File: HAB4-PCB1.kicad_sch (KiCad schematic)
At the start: 15 parts, among them J1 Barrel_Jack_Switch

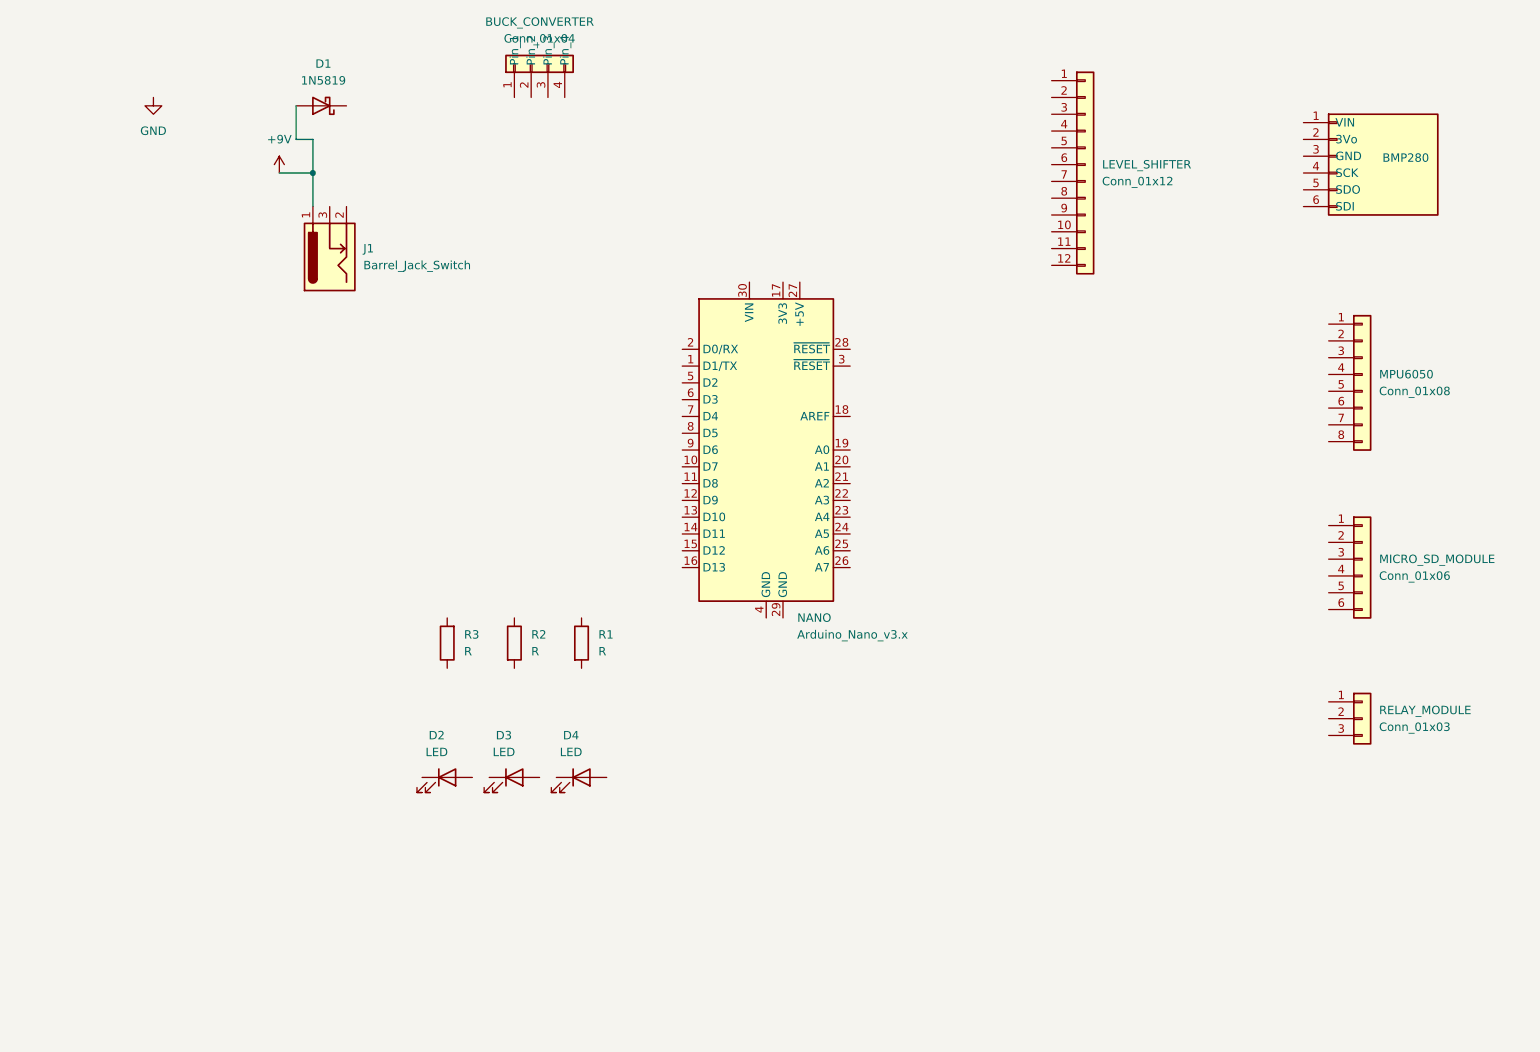
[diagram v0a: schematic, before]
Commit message: Connected modules
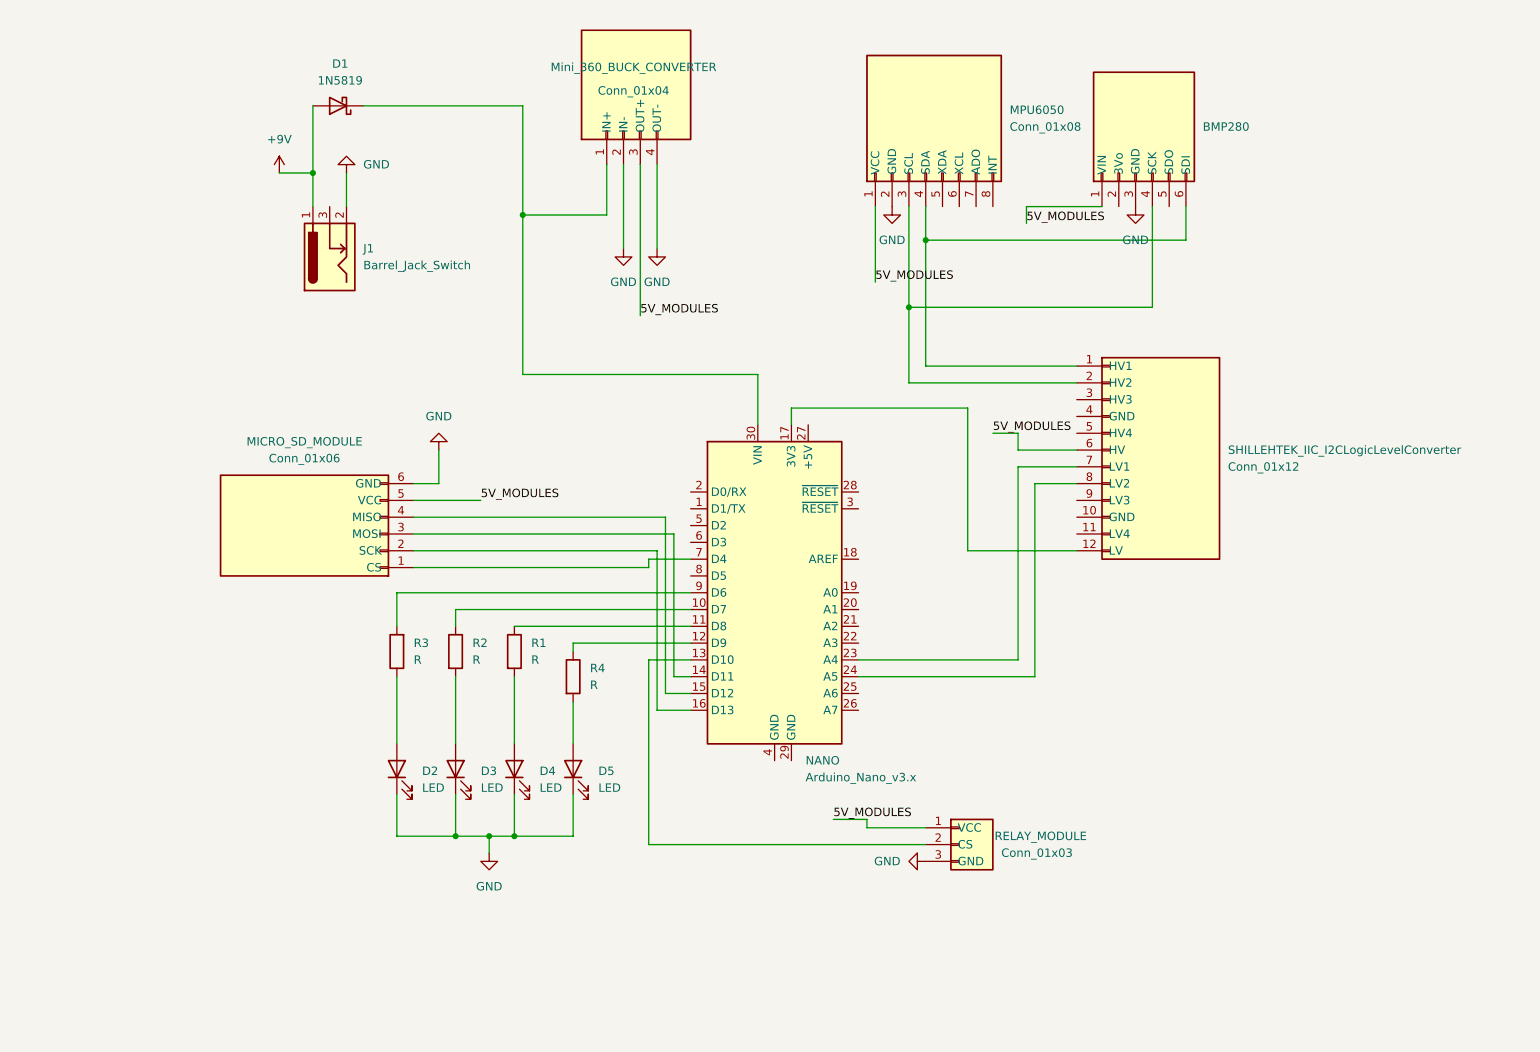
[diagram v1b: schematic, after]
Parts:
- added D5: LED, symbol Device:LED
- added R4: R, symbol Device:R
- renumbered BUCK_CONVERTER to Mini_360_BUCK_CONVERTER, LEVEL_SHIFTER to SHILLEHTEK_IIC_I2CLogicLevelConverter
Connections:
- net GND: now also BMP280.3 (GND), D2.1 (K), D3.1 (K), D4.1 (K), J1.2, MICRO_SD_MODULE.6 (GND), MPU6050.2 (GND), Mini_360_BUCK_CONVERTER.2 (IN-), Mini_360_BUCK_CONVERTER.4 (OUT-), RELAY_MODULE.3 (GND), D5.1 (K)
- net at R1.1: now also NANO.11 (D8)
- net at R1.2: now also D4.2 (A)
- net at SHILLEHTEK_IIC_I2CLogicLevelConverter.1 (HV1): now also BMP280.6 (SDI), MPU6050.4 (SDA)
- net at SHILLEHTEK_IIC_I2CLogicLevelConverter.12 (LV): now also NANO.17 (3V3)
- net at SHILLEHTEK_IIC_I2CLogicLevelConverter.2 (HV2): now also BMP280.4 (SCK), MPU6050.3 (SCL)
- net 5V_MODULES: now reaches SHILLEHTEK_IIC_I2CLogicLevelConverter.6 (HV)
- net 5V_MODULES: now also BMP280.1 (VIN), MICRO_SD_MODULE.5 (VCC), MPU6050.1 (VCC), Mini_360_BUCK_CONVERTER.3 (OUT+), RELAY_MODULE.1 (VCC)
- net at SHILLEHTEK_IIC_I2CLogicLevelConverter.7 (LV1): now also NANO.23 (A4)
- net at SHILLEHTEK_IIC_I2CLogicLevelConverter.8 (LV2): now also NANO.24 (A5)
- net at D1.1 (K): now also Mini_360_BUCK_CONVERTER.1 (IN+), NANO.30 (VIN)
- net at R2.1: now also NANO.10 (D7)
- net at R2.2: now also D3.2 (A)
- net at MICRO_SD_MODULE.1 (CS): now also NANO.7 (D4)
- net at MICRO_SD_MODULE.2 (SCK): now also NANO.16 (D13)
- net at MICRO_SD_MODULE.3 (MOSI): now also NANO.14 (D11)
- net at MICRO_SD_MODULE.4 (MISO): now also NANO.15 (D12)
- net at R3.1: now also D2.2 (A)
- net at R3.2: now also NANO.9 (D6)
- net at RELAY_MODULE.2 (CS): now also NANO.13 (D10)
- net at NANO.12 (D9): now also R4.1
- new net: D5.2 (A), R4.2
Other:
- moved on the sheet: BMP280, D1, D2, D3, D4, Mini_360_BUCK_CONVERTER, NANO, R1, R2, R3

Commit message: footprints and connections update
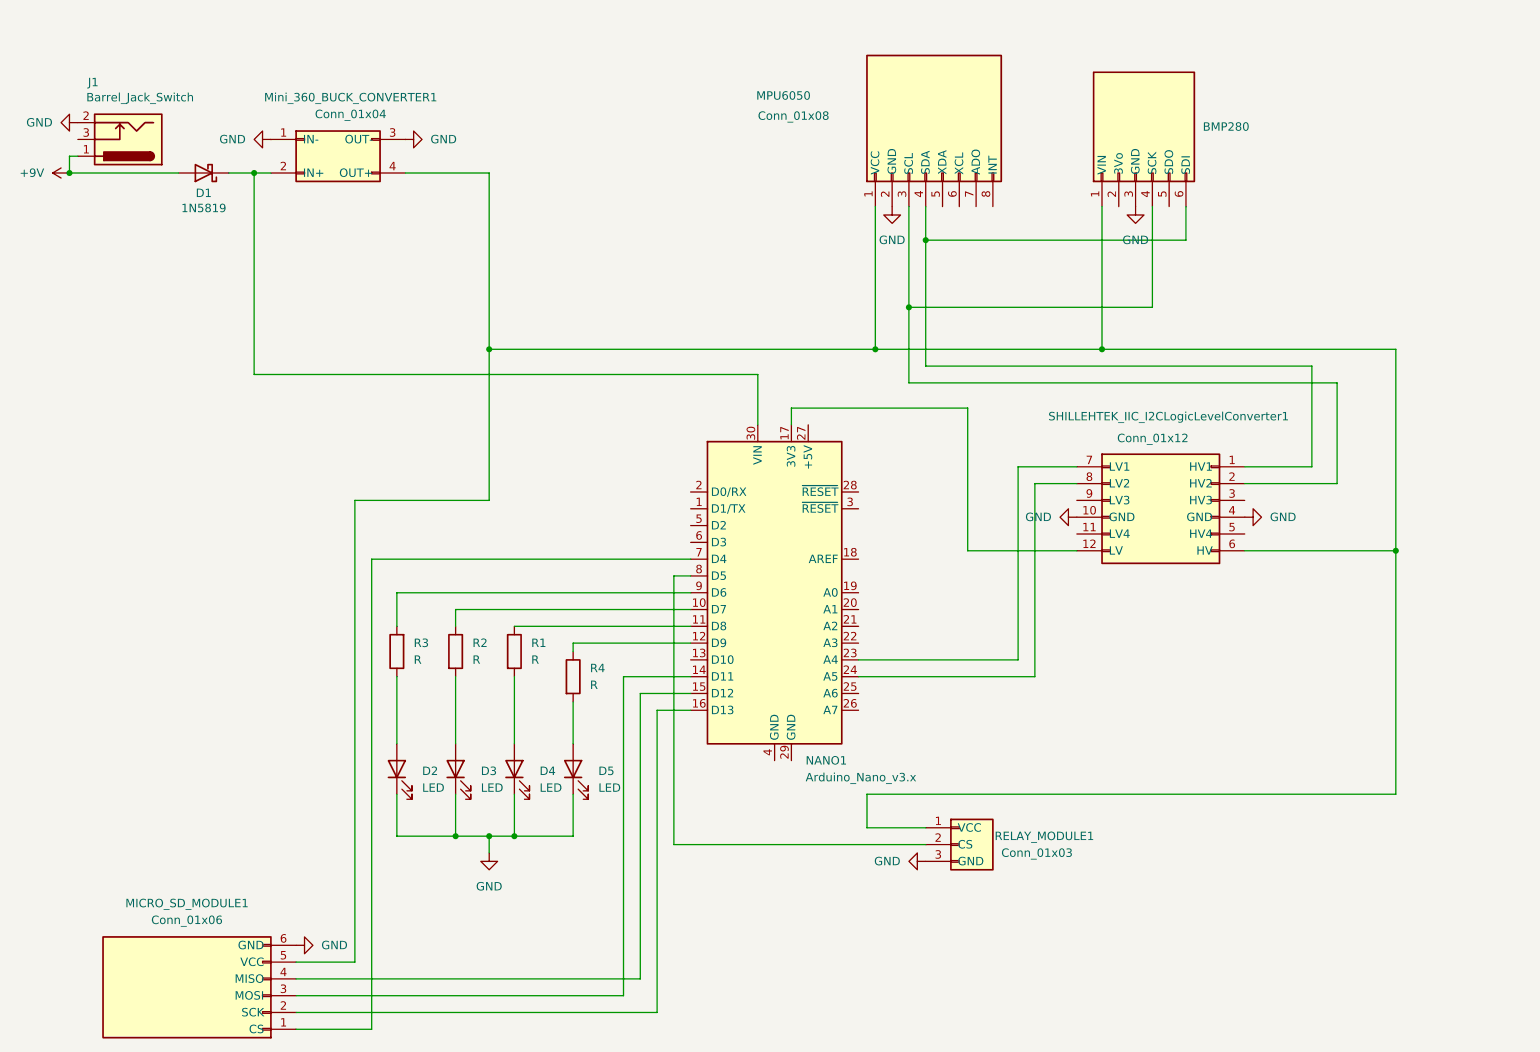
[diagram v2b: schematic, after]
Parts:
- BMP280: footprint (none) -> Connector_PinHeader_2.54mm:PinHeader_1x06_P2.54mm_Vertical
- D2, D3, D4, D5: footprint (none) -> LED_THT:LED_D5.0mm
- J1: footprint (none) -> Connector_BarrelJack:BarrelJack_CUI_PJ-063AH_Horizontal
- MICRO_SD_MODULE1: renamed from MICRO_SD_MODULE; footprint (none) -> Connector_PinHeader_2.54mm:PinHeader_1x06_P2.54mm_Vertical
- MPU6050: footprint (none) -> Connector_PinHeader_2.54mm:PinHeader_1x08_P2.54mm_Vertical
- Mini_360_BUCK_CONVERTER1: renamed from Mini_360_BUCK_CONVERTER; footprint (none) -> My_Footprints2:Buck_Module_4pin_12.7x17.78mm
- R1, R2, R3, R4: footprint (none) -> Resistor_THT:R_Axial_DIN0204_L3.6mm_D1.6mm_P5.08mm_Horizontal
- RELAY_MODULE1: renamed from RELAY_MODULE; footprint (none) -> Connector_PinHeader_2.54mm:PinHeader_1x03_P2.54mm_Vertical
- SHILLEHTEK_IIC_I2CLogicLevelConverter1: renamed from SHILLEHTEK_IIC_I2CLogicLevelConverter; footprint (none) -> My_Footprints2:I2C_LogicLevelConverter
- renumbered NANO to NANO1
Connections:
- net GND: now also Mini_360_BUCK_CONVERTER1.1 (IN-), Mini_360_BUCK_CONVERTER1.3 (OUT-), SHILLEHTEK_IIC_I2CLogicLevelConverter1.10 (GND), SHILLEHTEK_IIC_I2CLogicLevelConverter1.4 (GND); no longer Mini_360_BUCK_CONVERTER1.2 (IN-), Mini_360_BUCK_CONVERTER1.4 (OUT-)
- net at D1.1 (K), NANO1.30 (VIN): now also Mini_360_BUCK_CONVERTER1.2 (IN+); no longer Mini_360_BUCK_CONVERTER1.1 (IN+)
- net at RELAY_MODULE1.2 (CS): now also NANO1.8 (D5); no longer NANO1.13 (D10)
- net 5V_MODULES: no longer names the net of BMP280.1 (VIN), MICRO_SD_MODULE1.5 (VCC), MPU6050.1 (VCC), RELAY_MODULE1.1 (VCC), SHILLEHTEK_IIC_I2CLogicLevelConverter1.6 (HV)
- net 5V_MODULES: now also Mini_360_BUCK_CONVERTER1.4 (OUT+); no longer Mini_360_BUCK_CONVERTER1.3 (OUT+)
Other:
- moved on the sheet: D1, J1, MICRO_SD_MODULE1, Mini_360_BUCK_CONVERTER1, SHILLEHTEK_IIC_I2CLogicLevelConverter1

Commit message: pcb traces and remove relay
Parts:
- removed RELAY_MODULE1: Conn_01x03, Connector_PinHeader_2.54mm:PinHeader_1x03_P2.54mm_Vertical, symbol Connector_Generic:Conn_01x03
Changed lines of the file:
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@@
-	)
-	(junction
-		(at 218.44 97.79)
-		(diameter 0)
-		(color 0 0 0 0)
 	)
 	(junction
@@
 	(wire
 		(pts
-			(xy 109.22 101.6) (xy 109.22 142.24)
-		)
-		(stroke
-			(width 0)
-			(type default)
-		)
-	)
-	(wire
-		(pts
 			(xy 147.32 50.8) (xy 147.32 69.85)
 		)
@@
 	(wire
 		(pts
-			(xy 111.76 101.6) (xy 109.22 101.6)
-		)
-		(stroke
-			(width 0)
-			(type default)
-		)
-	)
-	(wire
-		(pts
 			(xy 111.76 104.14) (xy 67.31 104.14)
 		)
@@
 	(wire
 		(pts
-			(xy 138.43 134.62) (xy 138.43 139.7)
-		)
-		(stroke
-			(width 0)
-			(type default)
-		)
-	)
-	(wire
-		(pts
 			(xy 81.28 67.31) (xy 81.28 90.17)
 		)
@@
 	(wire
 		(pts
-			(xy 138.43 139.7) (xy 147.32 139.7)
-		)
-		(stroke
-			(width 0)
-			(type default)
-		)
-	)
-	(wire
-		(pts
 			(xy 81.28 140.97) (xy 76.2 140.97)
 		)
@@
 	(wire
 		(pts
-			(xy 138.43 134.62) (xy 218.44 134.62)
-		)
-		(stroke
-			(width 0)
-			(type default)
-		)
-	)
-	(wire
-		(pts
 			(xy 144.78 60.96) (xy 144.78 72.39)
 		)
@@
 	(wire
 		(pts
-			(xy 218.44 134.62) (xy 218.44 97.79)
-		)
-		(stroke
-			(width 0)
-			(type default)
-		)
-	)
-	(wire
-		(pts
 			(xy 195.58 85.09) (xy 205.74 85.09)
 		)
@@
 		(pts
 			(xy 106.68 167.64) (xy 106.68 121.92)
-		)
-		(stroke
-			(width 0)
-			(type default)
-		)
-	)
-	(wire
-		(pts
-			(xy 109.22 142.24) (xy 147.32 142.24)
 		)
 		(stroke
@@
 				(path "/01058913-1861-4ca7-a3f8-0ed56ef7e8c9"
 					(reference "R2")
-					(unit 1)
-				)
-			)
-		)
-	)
-	(symbol
-		(lib_id "power:GND")
-		(at 147.32 144.78 270)
-		(unit 1)
-		(exclude_from_sim no)
-		(in_bom yes)
-		(on_board yes)
-		(dnp no)
-		(fields_autoplaced yes)
-		(property "Reference" "#PWR08"
-			(at 140.97 144.78 0)
-			(effects
-				(font
-					(size 1.27 1.27)
-				)
-				(hide yes)
-			)
-		)
-		(property "Value" "GND"
-			(at 143.51 144.7799 90)
-			(effects
-				(font
-					(size 1.27 1.27)
-				)
-				(justify right)
-			)
-		)
-		(property "Footprint" ""
-			(at 147.32 144.78 0)
-			(effects
-				(font
-					(size 1.27 1.27)
-				)
-				(hide yes)
-			)
-		)
-		(property "Datasheet" ""
-			(at 147.32 144.78 0)
-			(effects
-				(font
-					(size 1.27 1.27)
-				)
-				(hide yes)
-			)
-		)
-		(property "Description" "Power symbol creates a global label with name \"GND\" , ground"
-			(at 147.32 144.78 0)
-			(effects
-				(font
-					(size 1.27 1.27)
-				)
-				(hide yes)
-			)
-		)
-		(pin "1"
-		)
-		(instances
-			(project "HAB4-PCB1"
-				(path "/01058913-1861-4ca7-a3f8-0ed56ef7e8c9"
-					(reference "#PWR08")
 					(unit 1)
 				)
@@
 					(unit 1)
 				)
-			)
-		)
-	)
-	(symbol
-		(lib_id "Connector_Generic:Conn_01x03")
-		(at 152.4 142.24 0)
-		(unit 1)
-		(exclude_from_sim no)
-		(in_bom yes)
-		(on_board yes)
-		(dnp no)
-		(fields_autoplaced yes)
-		(property "Reference" "RELAY_MODULE1"
-			(at 157.734 140.97 0)
-			(effects
-				(font
-					(size 1.27 1.27)
-				)
-				(justify left)
-			)
-		)
-		(property "Value" "Conn_01x03"
-			(at 158.75 143.51 0)
-			(effects
-				(font
-					(size 1.27 1.27)
-				)
-				(justify left)
-			)
-		)
-		(property "Footprint" "Connector_PinHeader_2.54mm:PinHeader_1x03_P2.54mm_Vertical"
-			(at 152.4 142.24 0)
-			(effects
-				(font
-					(size 1.27 1.27)
-				)
-				(hide yes)
-			)
-		)
-		(property "Datasheet" "~"
-			(at 152.4 142.24 0)
-			(effects
-				(font
-					(size 1.27 1.27)
-				)
-				(hide yes)
-			)
-		)
-		(property "Description" "Generic connector, single row, 01x03, script generated (kicad-library-utils/schlib/autogen/connector/)"
-			(at 152.4 142.24 0)
-			(effects
-				(font
-					(size 1.27 1.27)
-				)
-				(hide yes)
-			)
-		)
-		(pin "1"
-		)
-		(pin "2"
-		)
-		(pin "3"
-		)
-		(instances
-			(project ""
-				(path "/01058913-1861-4ca7-a3f8-0ed56ef7e8c9"
-					(reference "RELAY_MODULE1")
-					(unit 1)
-				)

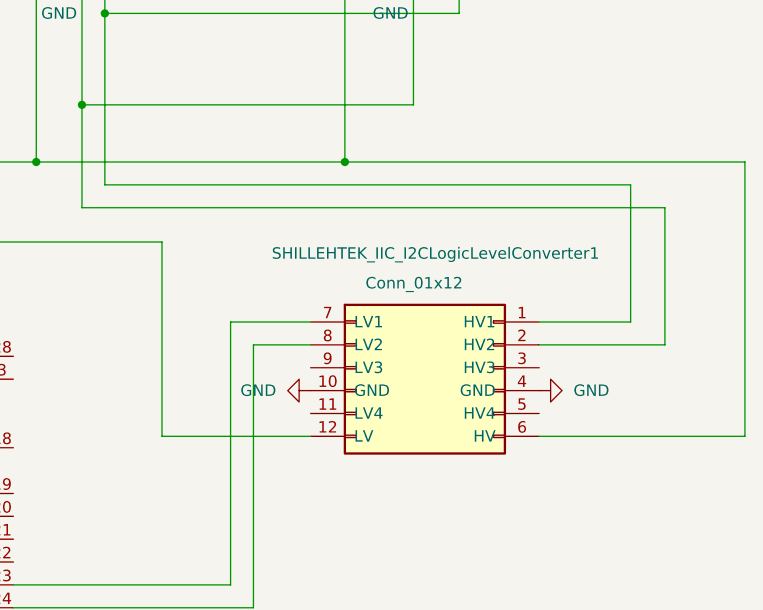
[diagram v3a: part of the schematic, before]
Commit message: Improve GND and fix Shifter pins
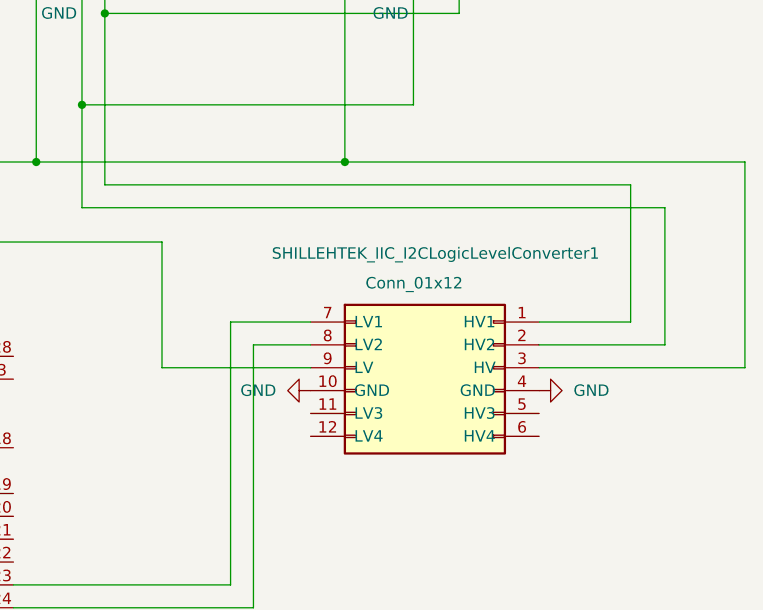
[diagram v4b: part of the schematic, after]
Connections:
- net at SHILLEHTEK_IIC_I2CLogicLevelConverter1.12 (LV4): no longer NANO1.17 (3V3)
- net at SHILLEHTEK_IIC_I2CLogicLevelConverter1.3 (HV): now also BMP280.1 (VIN), MICRO_SD_MODULE1.5 (VCC), MPU6050.1 (VCC), Mini_360_BUCK_CONVERTER1.4 (OUT+)
- net at SHILLEHTEK_IIC_I2CLogicLevelConverter1.9 (LV): now also NANO1.17 (3V3)
- now unconnected: SHILLEHTEK_IIC_I2CLogicLevelConverter1.6 (HV)
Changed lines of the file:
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@@
-	(wire
-		(pts
-			(xy 153.67 97.79) (xy 170.18 97.79)
-		)
-		(stroke
-			(width 0)
-			(type default)
-		)
-	)
 	(wire
 		(pts
@@
 	(wire
 		(pts
-			(xy 218.44 67.31) (xy 218.44 97.79)
-		)
-		(stroke
-			(width 0)
-			(type default)
-		)
-	)
-	(wire
-		(pts
 			(xy 17.78 38.1) (xy 19.05 38.1)
 		)
@@
 	(wire
 		(pts
+			(xy 195.58 90.17) (xy 218.44 90.17)
+		)
+		(stroke
+			(width 0)
+			(type default)
+		)
+	)
+	(wire
+		(pts
 			(xy 93.98 134.62) (xy 93.98 140.97)
 		)
@@
 	(wire
 		(pts
+			(xy 153.67 76.2) (xy 153.67 90.17)
+		)
+		(stroke
+			(width 0)
+			(type default)
+		)
+	)
+	(wire
+		(pts
 			(xy 144.78 60.96) (xy 144.78 72.39)
 		)
@@
 	(wire
 		(pts
-			(xy 195.58 97.79) (xy 218.44 97.79)
-		)
-		(stroke
-			(width 0)
-			(type default)
-		)
-	)
-	(wire
-		(pts
 			(xy 111.76 99.06) (xy 63.5 99.06)
 		)
@@
 	(wire
 		(pts
+			(xy 170.18 90.17) (xy 153.67 90.17)
+		)
+		(stroke
+			(width 0)
+			(type default)
+		)
+	)
+	(wire
+		(pts
 			(xy 173.99 67.31) (xy 139.7 67.31)
 		)
@@
 	(wire
 		(pts
-			(xy 153.67 76.2) (xy 153.67 97.79)
-		)
-		(stroke
-			(width 0)
-			(type default)
-		)
-	)
-	(wire
-		(pts
 			(xy 52.07 162.56) (xy 104.14 162.56)
 		)
@@
 		)
 		(stroke
+			(width 0)
+			(type default)
+		)
+	)
+	(wire
+		(pts
+			(xy 218.44 67.31) (xy 218.44 90.17)
+		)
+		(stroke

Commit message: Jumper cables and other
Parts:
- added JP1, JP2, JP4, JP5: Jumper_2_Bridged, My_Footprints2:6mm_jumper, symbol Jumper:Jumper_2_Bridged
- added JP3, JP6: Jumper_2_Bridged, My_Footprints2:8mm_jumper, symbol Jumper:Jumper_2_Bridged
- renumbered SHILLEHTEK_IIC_I2CLogicLevelConverter1 to I2C_LVL_SHIFTER1
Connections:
- net GND: now also NANO1.29 (GND), NANO1.4 (GND)
- net at R1.1: now also NANO1.9 (D6); no longer NANO1.11 (D8)
- net at BMP280.6 (SDI), MPU6050.4 (SDA): now also JP4.2 (B); no longer I2C_LVL_SHIFTER1.1 (HV1)
- net at BMP280.4 (SCK), I2C_LVL_SHIFTER1.2 (HV2): now also JP2.1 (A); no longer MPU6050.3 (SCL)
- net at I2C_LVL_SHIFTER1.7 (LV1): now also JP5.1 (A); no longer NANO1.23 (A4)
- net at D1.1 (K), Mini_360_BUCK_CONVERTER1.2 (IN+): now also JP1.1 (A); no longer NANO1.30 (VIN)
- net at R2.1: now also NANO1.8 (D5); no longer NANO1.10 (D7)
- net at R4.1: now also NANO1.10 (D7); no longer NANO1.12 (D9)
- net at MICRO_SD_MODULE1.1 (CS): now also JP3.2 (B); no longer NANO1.7 (D4)
- net at NANO1.15 (D12): now also JP6.1 (A); no longer MICRO_SD_MODULE1.4 (MISO)
- net at R3.2: now also NANO1.7 (D4); no longer NANO1.9 (D6)
- new net: JP5.2 (B), NANO1.23 (A4)
- new net: I2C_LVL_SHIFTER1.1 (HV1), JP4.1 (A)
- new net: JP2.2 (B), MPU6050.3 (SCL)
- new net: JP6.2 (B), MICRO_SD_MODULE1.4 (MISO)
- new net: JP3.1 (A), NANO1.11 (D8)
- new net: JP1.2 (B), NANO1.30 (VIN)
